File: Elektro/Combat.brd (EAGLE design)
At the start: 94 x 67 mm, 19 parts, among them IC1 MODUL_POLOLU, IC3 REG1117

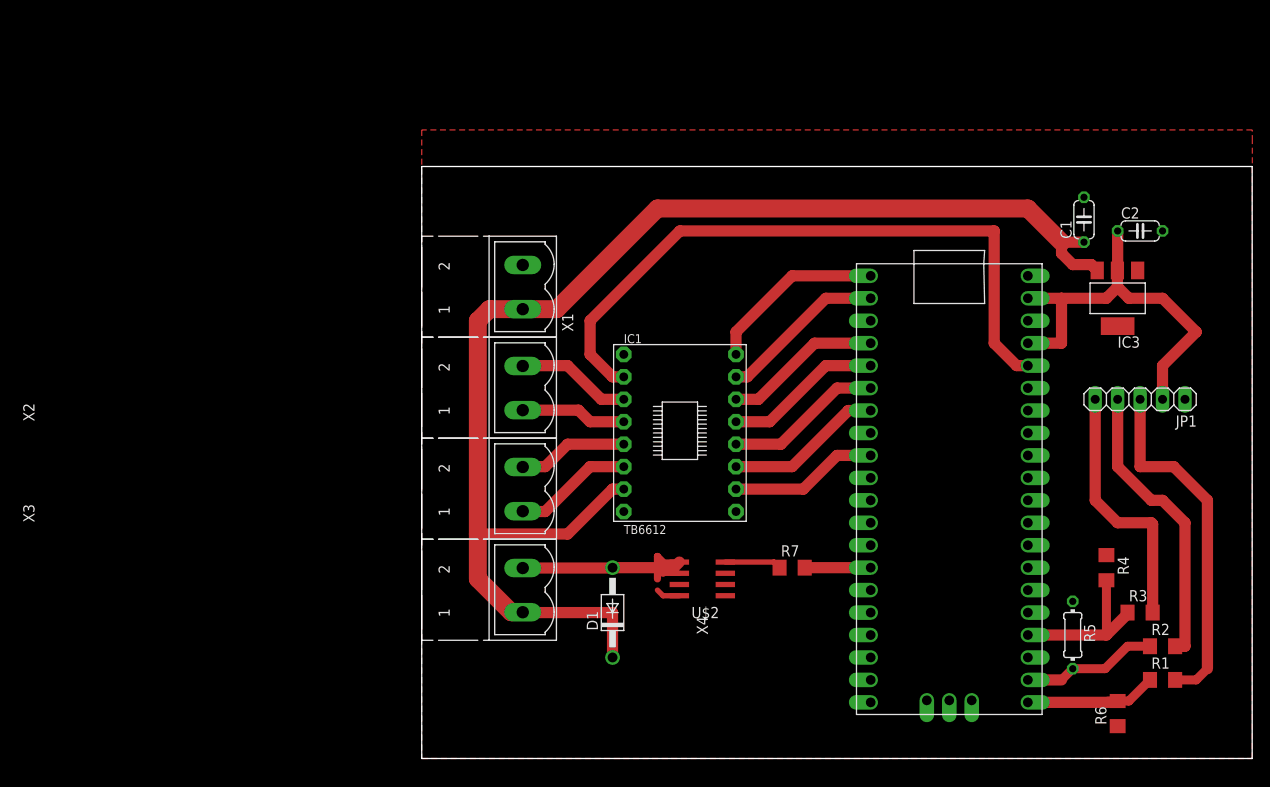
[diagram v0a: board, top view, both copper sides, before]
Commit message: making board smaller, SMD capacitators
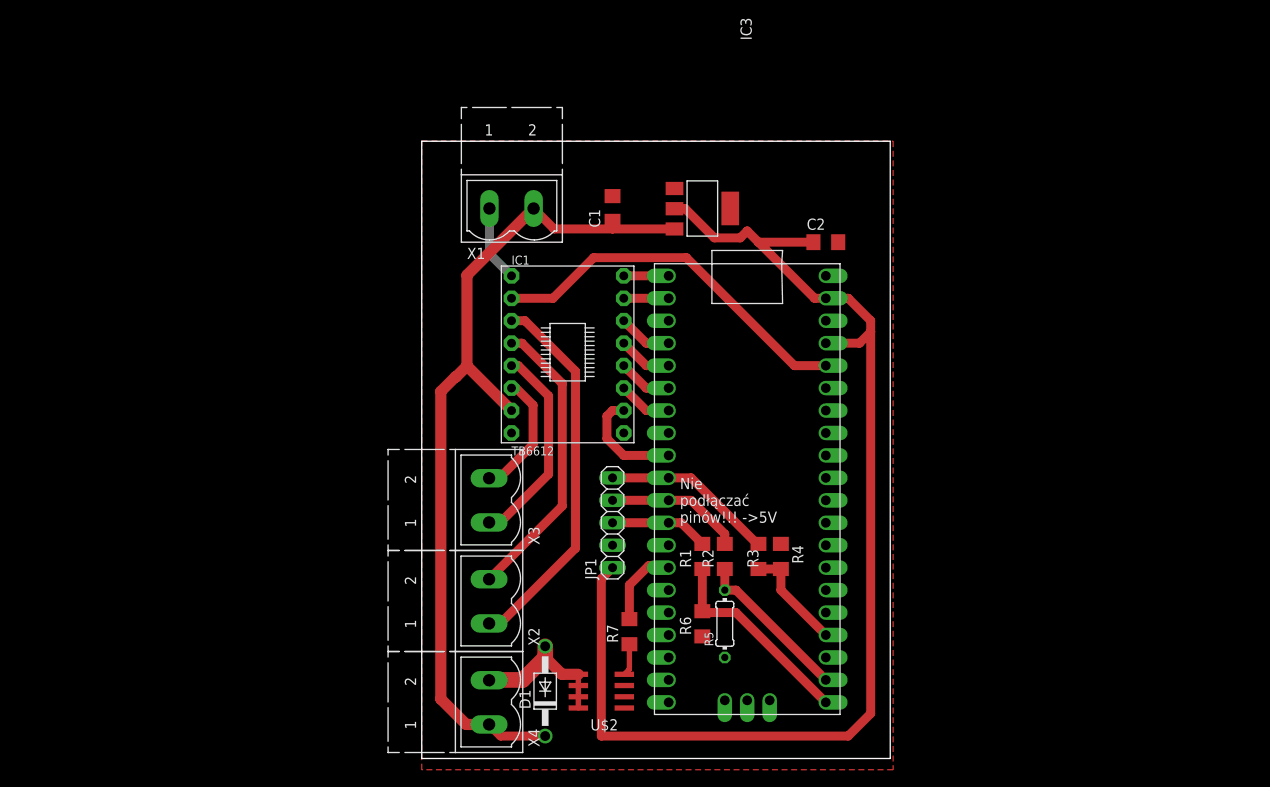
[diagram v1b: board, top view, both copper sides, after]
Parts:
- C1, C2: device rcl:C050-024X044 -> rcl:C1206
- moved JP1 61.3 mm to (21.6, 26.7), turned to 90 degrees
- moved R1 53.9 mm to (31.8, 22.9), turned to 90 degrees
- moved C1 53.4 mm to (21.6, 62.2)
- moved R2 50.6 mm to (34.3, 22.9), turned to 90 degrees
- moved IC3 48.1 mm to (31.8, 62.2), turned to 270 degrees
- moved R6 48.1 mm to (31.8, 15.2)
- moved R3 43.6 mm to (38.1, 22.9), turned to 90 degrees
- moved R5 39.4 mm to (34.3, 15.2), turned to 90 degrees
- moved R4 36.9 mm to (40.6, 22.9)
- moved C2 35.6 mm to (45.7, 58.4)
- moved X2 24.4 mm to (7.62, 17.8)
- moved U$1 22.9 mm to (36.8, 30.5)
- moved R7 19.8 mm to (23.5, 14.4), turned to 90 degrees
- moved U$2 17.1 mm to (20.3, 7.62)
- moved IC1 15.5 mm to (16.5, 45.7)
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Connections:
- net +5V: now also JP1.1; no longer JP1.2
- net AO1: now also X2.1; no longer X2.2
- net AO2: now also X2.2; no longer X2.1
- net BO1: now also X3.2; no longer X3.1
- net BO2: now also X3.1; no longer X3.2
- net GND: now also JP1.2, X1.1; no longer JP1.1, X1.2
- net N$1: now also U$1.GP9
- net N$2: now also U$1.GP8
- net N$3: now also U$1.GP7
- net V+: now also X1.2; no longer X1.1
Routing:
- net +5V: track 46.1 -> 135.5 mm
- net V+: track 151.6 -> 98.4 mm
- net +3V3: track 76.2 -> 42.5 mm
- net AO1: track 13.0 -> 42.9 mm
- net N$1: track 40.1 -> 11.1 mm
- net AO2: track 12.0 -> 33.2 mm
- net N$2: track 33.0 -> 15.4 mm
- net PWMA: track 20.4 -> 5.08 mm
- net AIN1: track 18.9 -> 5.08 mm
- net DC_DRIVE_ON: track 17.9 -> 6.13 mm
- net AIN2: track 17.9 -> 6.13 mm
- net BIN2: track 17.9 -> 6.13 mm
- net BIN1: track 17.9 -> 6.13 mm
- net N$4: track 28.8 -> 17.0 mm
- net BO2: track 12.5 -> 23.5 mm
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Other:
- board size 94 x 67 mm -> 53 x 69.8 mm
- board text added: "Nie podłączać pinów!!! ->5V"
